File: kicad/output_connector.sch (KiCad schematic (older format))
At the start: 2 parts, among them J4 PJ-079BH, J5 OUT

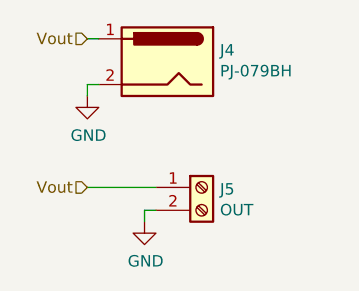
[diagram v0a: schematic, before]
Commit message: Updated schematic
Made some error with first rev, the found error are now corrected.
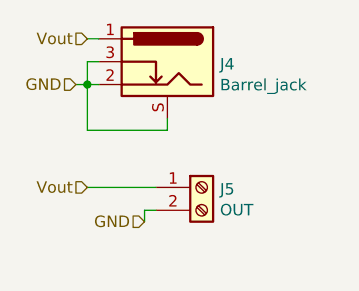
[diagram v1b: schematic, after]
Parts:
- removed J4: PJ-079BH, symbol Connector:Jack-DC
- added J4: Barrel_jack, connectors:PJ079BH, symbol connector:Barrel_jack
- J5: footprint (none) -> connectors:TerminalBlock_02_P5.00mm
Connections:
- net GND: now also J4.2, J4.3, J4.S (Shield)
- net Vout: now also J4.1
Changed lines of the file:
@@
 $Descr A4 11693 8268
 encoding utf-8
-Sheet 6 6
+Sheet 5 7
 Title ""
 Date ""
@@
 F 0 "J5" H 6580 3442 50  0000 L CNN
 F 1 "OUT" H 6580 3351 50  0000 L CNN
-F 2 "" H 6500 3450 50  0001 C CNN
+F 2 "connectors:TerminalBlock_02_P5.00mm" H 6500 3450 50  0001 C CNN
 F 3 "~" H 6500 3450 50  0001 C CNN
 	1    6500 3450
@@
 Wire Wire Line
 	6000 3450 6300 3450
-$Comp
-L power:GND #PWR0129
-U 1 1 5FD866D5
-P 6250 3600
-F 0 "#PWR0129" H 6250 3350 50  0001 C CNN
-F 1 "GND" H 6255 3427 50  0000 C CNN
-F 2 "" H 6250 3600 50  0001 C CNN
-F 3 "" H 6250 3600 50  0001 C CNN
-	1    6250 3600
-	1    0    0    -1
-$EndComp
 Wire Wire Line
 	6250 3600 6250 3550
 Wire Wire Line
 	6250 3550 6300 3550
+Wire Wire Line
+	6050 3000 6000 3000
+Text HLabel 6250 3600 0    50   Input ~ 0
+GND
+Text HLabel 5950 3000 0    50   Input ~ 0
+GND
 $Comp
-L Connector:Jack-DC J4
-U 1 1 5FD9FE96
+L connector:Barrel_jack J4
+U 1 1 5FC6D75C
 P 6350 2900
-F 0 "J4" H 6120 2950 50  0000 R CNN
-F 1 "PJ-079BH" H 6120 2859 50  0000 R CNN
-F 2 "" H 6400 2860 50  0001 C CNN
+F 0 "J4" H 6120 2889 50  0000 R CNN
+F 1 "Barrel_jack" H 6120 2798 50  0000 R CNN
+F 2 "connectors:PJ079BH" H 6400 2860 50  0001 C CNN
 F 3 "~" H 6400 2860 50  0001 C CNN
 	1    6350 2900
 	-1   0    0    -1
 $EndComp
+Wire Wire Line
+	6050 2800 6000 2800
 Text HLabel 6000 2800 0    50   Input ~ 0
 Vout
-$Comp
-L power:GND #PWR0130
-U 1 1 5FDA0E01
-P 6000 3050
-F 0 "#PWR0130" H 6000 2800 50  0001 C CNN
-F 1 "GND" H 6005 2877 50  0000 C CNN
-F 2 "" H 6000 3050 50  0001 C CNN
-F 3 "" H 6000 3050 50  0001 C CNN
-	1    6000 3050
-	1    0    0    -1
-$EndComp
 Wire Wire Line
-	6050 3000 6000 3000
+	6050 2900 6000 2900
 Wire Wire Line
-	6000 3000 6000 3050
+	6000 2900 6000 3000
+Connection ~ 6000 3000
 Wire Wire Line
-	6050 2800 6000 2800
+	6000 3000 5950 3000
+Wire Wire Line
+	6000 3000 6000 3200
+Wire Wire Line
+	6000 3200 6350 3200
+Wire Wire Line
+	6350 3200 6350 3150
 $EndSCHEMATC
